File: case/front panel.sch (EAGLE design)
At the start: 3 parts

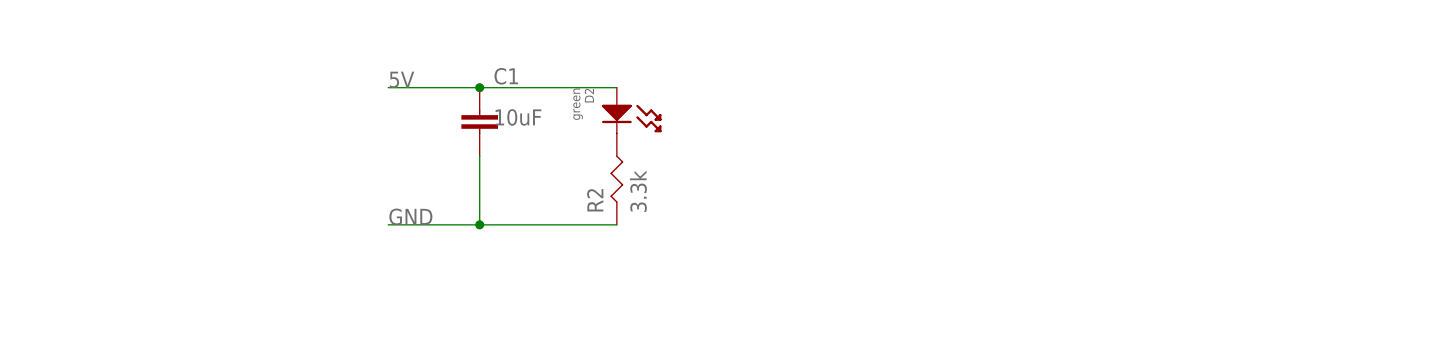
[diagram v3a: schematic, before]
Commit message: add rgb leds
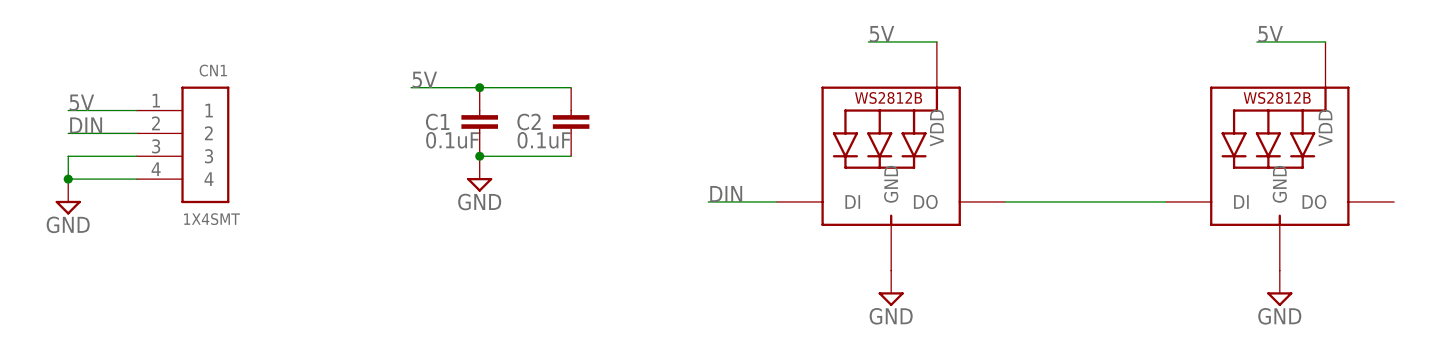
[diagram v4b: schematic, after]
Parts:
- removed D2: green, MF_LEDs:LED_SINGLE-0805
- removed R2: 3.3k, FlashPCB_Resistors:RES-0402
- added C2: 0.1uF, Nordic_nRF:CAPACITOR_0805_N
- added CN1: 1X4SMT, adafruit:1X4SMT
- added LED1, LED2: WS2812B_5050N, adafruit:WS2812B_5050N
- C1: value 10uF -> 0.1uF
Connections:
- new net DIN: CN1.2, LED1.DI
- net 5V: now also C2.1, CN1.1, LED1.VDD, LED2.VDD; no longer D2.ANODE
- net GND: now also C2.2, CN1.3, CN1.4, LED1.GND, LED2.GND; no longer R2.P$1
- net N$2: now also LED1.DO, LED2.DI; no longer D2.CATHODE, R2.P$2
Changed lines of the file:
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@@
 </classes>
 <parts>
-<part name="D2" library="MF_LEDs" deviceset="LED_SINGLE" device="-0805" value="green"/>
-<part name="R2" library="FlashPCB_Resistors" deviceset="RES-0402" device="" value="3.3k"/>
-<part name="C1" library="Nordic_nRF" library_urn="urn:adsk.eagle:library:169009" deviceset="CAPACITOR" device="_0805_N" package3d_urn="urn:adsk.eagle:package:2593736/1" value="10uF"/>
+<part name="C1" library="Nordic_nRF" library_urn="urn:adsk.eagle:library:169009" deviceset="CAPACITOR" device="_0805_N" package3d_urn="urn:adsk.eagle:package:2593736/1" value="0.1uF"/>
+<part name="LED1" library="adafruit" deviceset="WS2812B" device="_5050N"/>
+<part name="LED2" library="adafruit" deviceset="WS2812B" device="_5050N"/>
+<part name="SUPPLY1" library="Power_Symbols" library_urn="urn:adsk.eagle:library:16502351" deviceset="GND" device="" value="GND"/>
+<part name="SUPPLY2" library="Power_Symbols" library_urn="urn:adsk.eagle:library:16502351" deviceset="GND" device="" value="GND"/>
+<part name="SUPPLY3" library="Power_Symbols" library_urn="urn:adsk.eagle:library:16502351" deviceset="GND" device="" value="GND"/>
+<part name="CN1" library="adafruit" deviceset="1X4" device="SMT"/>
+<part name="SUPPLY4" library="Power_Symbols" library_urn="urn:adsk.eagle:library:16502351" deviceset="GND" device="" value="GND"/>
+<part name="C2" library="Nordic_nRF" library_urn="urn:adsk.eagle:library:169009" deviceset="CAPACITOR" device="_0805_N" package3d_urn="urn:adsk.eagle:package:2593736/1" value="0.1uF"/>
 </parts>
 <sheets>
@@
 </plain>
 <instances>
-<instance part="D2" gate="G$1" x="38.1" y="27.94" smashed="yes" rot="R270">
-<attribute name="NAME" x="35.56" y="30.48" size="1.016" layer="95" font="vector" rot="R270" align="top-left"/>
-<attribute name="VALUE" x="33.02" y="30.48" size="1.016" layer="96" font="vector" rot="R270"/>
+<instance part="C1" gate="C$1" x="22.86" y="27.94" smashed="yes">
+<attribute name="NAME" x="16.764" y="25.781" size="1.778" layer="95"/>
+<attribute name="VALUE" x="16.764" y="23.749" size="1.778" layer="96"/>
 </instance>
-<instance part="R2" gate="G$1" x="38.1" y="20.32" smashed="yes" rot="R90">
-<attribute name="NAME" x="36.6014" y="16.51" size="1.778" layer="95" rot="R90"/>
-<attribute name="VALUE" x="41.402" y="16.51" size="1.778" layer="96" rot="R90"/>
+<instance part="LED1" gate="G$1" x="68.58" y="20.32" smashed="yes"/>
+<instance part="LED2" gate="G$1" x="111.76" y="20.32" smashed="yes"/>
+<instance part="SUPPLY1" gate="G$1" x="22.86" y="20.32" smashed="yes">
+<attribute name="VALUE" x="22.86" y="17.78" size="1.778" layer="96" align="center"/>
 </instance>
-<instance part="C1" gate="C$1" x="22.86" y="27.94" smashed="yes">
-<attribute name="NAME" x="24.384" y="30.861" size="1.778" layer="95"/>
-<attribute name="VALUE" x="24.384" y="26.289" size="1.778" layer="96"/>
+<instance part="SUPPLY2" gate="G$1" x="68.58" y="7.62" smashed="yes">
+<attribute name="VALUE" x="68.58" y="5.08" size="1.778" layer="96" align="center"/>
+</instance>
+<instance part="SUPPLY3" gate="G$1" x="111.76" y="7.62" smashed="yes">
+<attribute name="VALUE" x="111.76" y="5.08" size="1.778" layer="96" align="center"/>
+</instance>
+<instance part="CN1" gate="G$1" x="-10.16" y="25.4" smashed="yes">
+<attribute name="NAME" x="-5.08" y="33.02" size="1.27" layer="95" font="vector" rot="R180"/>
+<attribute name="VALUE" x="-10.16" y="15.24" size="1.27" layer="96" font="vector"/>
+</instance>
+<instance part="SUPPLY4" gate="G$1" x="-22.86" y="17.78" smashed="yes">
+<attribute name="VALUE" x="-22.86" y="15.24" size="1.778" layer="96" align="center"/>
+</instance>
+<instance part="C2" gate="C$1" x="33.02" y="27.94" smashed="yes">
+<attribute name="NAME" x="26.924" y="25.781" size="1.778" layer="95"/>
+<attribute name="VALUE" x="26.924" y="23.749" size="1.778" layer="96"/>
 </instance>
 </instances>
@@
 <net name="GND" class="0">
 <segment>
-<pinref part="R2" gate="G$1" pin="P$1"/>
-<wire x1="38.1" y1="15.24" x2="22.86" y2="15.24" width="0.1524" layer="91"/>
-<wire x1="22.86" y1="15.24" x2="12.7" y2="15.24" width="0.1524" layer="91"/>
-<wire x1="22.86" y1="22.86" x2="22.86" y2="15.24" width="0.1524" layer="91"/>
-<junction x="22.86" y="15.24"/>
 <pinref part="C1" gate="C$1" pin="2"/>
-<label x="12.7" y="15.24" size="1.778" layer="95"/>
+<pinref part="SUPPLY1" gate="G$1" pin="GND"/>
+<pinref part="C2" gate="C$1" pin="2"/>
+<wire x1="33.02" y1="22.86" x2="22.86" y2="22.86" width="0.1524" layer="91"/>
+<junction x="22.86" y="22.86"/>
+</segment>
+<segment>
+<pinref part="LED1" gate="G$1" pin="GND"/>
+<pinref part="SUPPLY2" gate="G$1" pin="GND"/>
+</segment>
+<segment>
+<pinref part="LED2" gate="G$1" pin="GND"/>
+<pinref part="SUPPLY3" gate="G$1" pin="GND"/>
+</segment>
+<segment>
+<pinref part="CN1" gate="G$1" pin="4"/>
+<wire x1="-15.24" y1="20.32" x2="-22.86" y2="20.32" width="0.1524" layer="91"/>
+<pinref part="SUPPLY4" gate="G$1" pin="GND"/>
+<pinref part="CN1" gate="G$1" pin="3"/>
+<wire x1="-15.24" y1="22.86" x2="-22.86" y2="22.86" width="0.1524" layer="91"/>
+<wire x1="-22.86" y1="22.86" x2="-22.86" y2="20.32" width="0.1524" layer="91"/>
+<junction x="-22.86" y="20.32"/>
 </segment>
 </net>
 <net name="5V" class="0">
 <segment>
-<pinref part="D2" gate="G$1" pin="ANODE"/>
-<wire x1="38.1" y1="30.48" x2="22.86" y2="30.48" width="0.1524" layer="91"/>
 <pinref part="C1" gate="C$1" pin="1"/>
-<wire x1="22.86" y1="30.48" x2="12.7" y2="30.48" width="0.1524" layer="91"/>
+<wire x1="22.86" y1="30.48" x2="15.24" y2="30.48" width="0.1524" layer="91"/>
+<label x="15.24" y="30.48" size="1.778" layer="95"/>
+<pinref part="C2" gate="C$1" pin="1"/>
+<wire x1="22.86" y1="30.48" x2="33.02" y2="30.48" width="0.1524" layer="91"/>
 <junction x="22.86" y="30.48"/>
-<label x="12.7" y="30.48" size="1.778" layer="95"/>
 </segment>
-</net>
-<net name="N$1" class="0">
+<segment>
+<pinref part="LED2" gate="G$1" pin="VDD"/>
+<wire x1="116.84" y1="35.56" x2="109.22" y2="35.56" width="0.1524" layer="91"/>
+<label x="109.22" y="35.56" size="1.778" layer="95"/>
+</segment>
+<segment>
+<pinref part="LED1" gate="G$1" pin="VDD"/>
+<wire x1="73.66" y1="35.56" x2="66.04" y2="35.56" width="0.1524" layer="91"/>
+<label x="66.04" y="35.56" size="1.778" layer="95"/>
+</segment>
+<segment>
+<pinref part="CN1" gate="G$1" pin="1"/>
+<wire x1="-15.24" y1="27.94" x2="-22.86" y2="27.94" width="0.1524" layer="91"/>
+<label x="-22.86" y="27.94" size="1.778" layer="95"/>
+</segment>
 </net>
 <net name="N$2" class="0">
 <segment>
-<pinref part="R2" gate="G$1" pin="P$2"/>
-<pinref part="D2" gate="G$1" pin="CATHODE"/>
+<pinref part="LED1" gate="G$1" pin="DO"/>
+<pinref part="LED2" gate="G$1" pin="DI"/>
+<wire x1="81.28" y1="17.78" x2="99.06" y2="17.78" width="0.1524" layer="91"/>
 </segment>
 </net>
+<net name="DIN" class="0">
+<segment>
+<pinref part="CN1" gate="G$1" pin="2"/>
+<wire x1="-15.24" y1="25.4" x2="-22.86" y2="25.4" width="0.1524" layer="91"/>
+<label x="-22.86" y="25.4" size="1.778" layer="95"/>
+</segment>
+<segment>
+<pinref part="LED1" gate="G$1" pin="DI"/>
+<wire x1="55.88" y1="17.78" x2="48.26" y2="17.78" width="0.1524" layer="91"/>
+<label x="48.26" y="17.78" size="1.778" layer="95"/>
+</segment>
+</net>

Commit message: use SK6812MINI-E leds
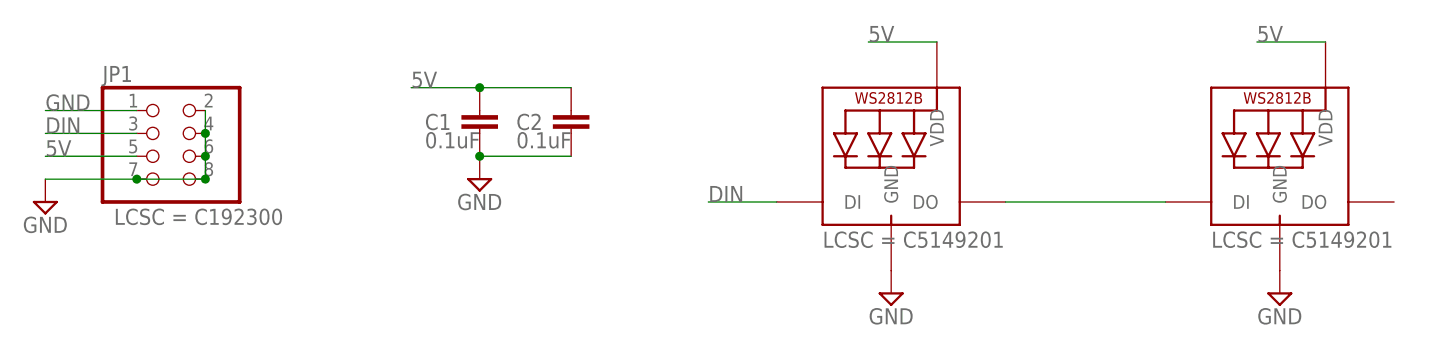
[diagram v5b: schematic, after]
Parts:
- removed CN1: 1X4SMT, adafruit:1X4SMT
- removed LED2: WS2812B_5050N, adafruit:WS2812B_5050N
- added JP1: connect, pinhead+:PINHD-2X4SMT
- added LED0: WS2812B_SK6812E, microbuilder:WS2812B_SK6812E
- LED1: value WS2812B_5050N -> WS2812B_SK6812E; device adafruit:WS2812B_5050N -> microbuilder:WS2812B_SK6812E; LCSC (none) -> C5149201
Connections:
- net 5V: now also JP1.5, LED0.VDD; no longer CN1.1, LED2.VDD
- net DIN: now also JP1.3; no longer CN1.2
- net GND: now also JP1.1, JP1.2, JP1.4, JP1.6, JP1.7, JP1.8, LED0.GND; no longer CN1.3, CN1.4, LED2.GND
- net N$2: now also LED0.DI; no longer LED2.DI
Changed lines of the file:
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@@
 <layer number="59" name="tCarbon" color="7" fill="1" visible="no" active="no"/>
 <layer number="60" name="bCarbon" color="7" fill="1" visible="no" active="no"/>
+<layer number="61" name="stand" color="7" fill="1" visible="no" active="no"/>
 <layer number="88" name="SimResults" color="9" fill="1" visible="yes" active="yes"/>
 <layer number="89" name="SimProbes" color="9" fill="1" visible="yes" active="yes"/>
@@
 <parts>
 <part name="C1" library="Nordic_nRF" library_urn="urn:adsk.eagle:library:169009" deviceset="CAPACITOR" device="_0805_N" package3d_urn="urn:adsk.eagle:package:2593736/1" value="0.1uF"/>
-<part name="LED1" library="adafruit" deviceset="WS2812B" device="_5050N"/>
-<part name="LED2" library="adafruit" deviceset="WS2812B" device="_5050N"/>
 <part name="SUPPLY1" library="Power_Symbols" library_urn="urn:adsk.eagle:library:16502351" deviceset="GND" device="" value="GND"/>
 <part name="SUPPLY2" library="Power_Symbols" library_urn="urn:adsk.eagle:library:16502351" deviceset="GND" device="" value="GND"/>
 <part name="SUPPLY3" library="Power_Symbols" library_urn="urn:adsk.eagle:library:16502351" deviceset="GND" device="" value="GND"/>
-<part name="CN1" library="adafruit" deviceset="1X4" device="SMT"/>
 <part name="SUPPLY4" library="Power_Symbols" library_urn="urn:adsk.eagle:library:16502351" deviceset="GND" device="" value="GND"/>
 <part name="C2" library="Nordic_nRF" library_urn="urn:adsk.eagle:library:169009" deviceset="CAPACITOR" device="_0805_N" package3d_urn="urn:adsk.eagle:package:2593736/1" value="0.1uF"/>
+<part name="LED1" library="microbuilder" deviceset="WS2812B" device="_SK6812E">
+<attribute name="LCSC" value="C5149201"/>
+</part>
+<part name="LED0" library="microbuilder" deviceset="WS2812B" device="_SK6812E">
+<attribute name="LCSC" value="C5149201"/>
+</part>
+<part name="JP1" library="pinhead+" deviceset="PINHD-2X4" device="SMT" value="connect">
+<attribute name="LCSC" value="C192300"/>
+</part>
 </parts>
 <sheets>
@@
 <attribute name="VALUE" x="16.764" y="23.749" size="1.778" layer="96"/>
 </instance>
-<instance part="LED1" gate="G$1" x="68.58" y="20.32" smashed="yes"/>
-<instance part="LED2" gate="G$1" x="111.76" y="20.32" smashed="yes"/>
 <instance part="SUPPLY1" gate="G$1" x="22.86" y="20.32" smashed="yes">
 <attribute name="VALUE" x="22.86" y="17.78" size="1.778" layer="96" align="center"/>
@@
 <attribute name="VALUE" x="111.76" y="5.08" size="1.778" layer="96" align="center"/>
 </instance>
-<instance part="CN1" gate="G$1" x="-10.16" y="25.4" smashed="yes">
-<attribute name="NAME" x="-5.08" y="33.02" size="1.27" layer="95" font="vector" rot="R180"/>
-<attribute name="VALUE" x="-10.16" y="15.24" size="1.27" layer="96" font="vector"/>
-</instance>
-<instance part="SUPPLY4" gate="G$1" x="-22.86" y="17.78" smashed="yes">
-<attribute name="VALUE" x="-22.86" y="15.24" size="1.778" layer="96" align="center"/>
+<instance part="SUPPLY4" gate="G$1" x="-25.4" y="17.78" smashed="yes">
+<attribute name="VALUE" x="-25.4" y="15.24" size="1.778" layer="96" align="center"/>
 </instance>
 <instance part="C2" gate="C$1" x="33.02" y="27.94" smashed="yes">
 <attribute name="NAME" x="26.924" y="25.781" size="1.778" layer="95"/>
 <attribute name="VALUE" x="26.924" y="23.749" size="1.778" layer="96"/>
+</instance>
+<instance part="LED1" gate="G$1" x="68.58" y="20.32" smashed="yes">
+<attribute name="LCSC" x="60.96" y="12.7" size="1.778" layer="96" display="both"/>
+</instance>
+<instance part="LED0" gate="G$1" x="111.76" y="20.32" smashed="yes">
+<attribute name="LCSC" x="104.14" y="12.7" size="1.778" layer="96" display="both"/>
+</instance>
+<instance part="JP1" gate="A" x="-12.7" y="22.86" smashed="yes">
+<attribute name="NAME" x="-19.05" y="31.115" size="1.778" layer="95"/>
+<attribute name="LCSC" x="-17.78" y="15.24" size="1.778" layer="96" display="both"/>
 </instance>
 </instances>
@@
 </segment>
 <segment>
+<wire x1="-15.24" y1="20.32" x2="-25.4" y2="20.32" width="0.1524" layer="91"/>
+<pinref part="SUPPLY4" gate="G$1" pin="GND"/>
+<pinref part="JP1" gate="A" pin="7"/>
+<pinref part="JP1" gate="A" pin="2"/>
+<pinref part="JP1" gate="A" pin="4"/>
+<wire x1="-7.62" y1="27.94" x2="-7.62" y2="25.4" width="0.1524" layer="91"/>
+<pinref part="JP1" gate="A" pin="6"/>
+<wire x1="-7.62" y1="25.4" x2="-7.62" y2="22.86" width="0.1524" layer="91"/>
+<junction x="-7.62" y="25.4"/>
+<pinref part="JP1" gate="A" pin="8"/>
+<wire x1="-7.62" y1="22.86" x2="-7.62" y2="20.32" width="0.1524" layer="91"/>
+<junction x="-7.62" y="22.86"/>
+<wire x1="-7.62" y1="20.32" x2="-15.24" y2="20.32" width="0.1524" layer="91"/>
+<junction x="-7.62" y="20.32"/>
+<junction x="-15.24" y="20.32"/>
+</segment>
+<segment>
 <pinref part="LED1" gate="G$1" pin="GND"/>
 <pinref part="SUPPLY2" gate="G$1" pin="GND"/>
 </segment>
 <segment>
-<pinref part="LED2" gate="G$1" pin="GND"/>
 <pinref part="SUPPLY3" gate="G$1" pin="GND"/>
-</segment>
-<segment>
-<pinref part="CN1" gate="G$1" pin="4"/>
-<wire x1="-15.24" y1="20.32" x2="-22.86" y2="20.32" width="0.1524" layer="91"/>
-<pinref part="SUPPLY4" gate="G$1" pin="GND"/>
-<pinref part="CN1" gate="G$1" pin="3"/>
-<wire x1="-15.24" y1="22.86" x2="-22.86" y2="22.86" width="0.1524" layer="91"/>
-<wire x1="-22.86" y1="22.86" x2="-22.86" y2="20.32" width="0.1524" layer="91"/>
-<junction x="-22.86" y="20.32"/>
+<pinref part="LED0" gate="G$1" pin="GND"/>
+</segment>
+<segment>
+<wire x1="-15.24" y1="27.94" x2="-25.4" y2="27.94" width="0.1524" layer="91"/>
+<label x="-25.4" y="27.94" size="1.778" layer="95"/>
+<pinref part="JP1" gate="A" pin="1"/>
 </segment>
 </net>
@@
 </segment>
 <segment>
-<pinref part="LED2" gate="G$1" pin="VDD"/>
 <wire x1="116.84" y1="35.56" x2="109.22" y2="35.56" width="0.1524" layer="91"/>
 <label x="109.22" y="35.56" size="1.778" layer="95"/>
-</segment>
-<segment>
-<pinref part="LED1" gate="G$1" pin="VDD"/>
+<pinref part="LED0" gate="G$1" pin="VDD"/>
+</segment>
+<segment>
 <wire x1="73.66" y1="35.56" x2="66.04" y2="35.56" width="0.1524" layer="91"/>
 <label x="66.04" y="35.56" size="1.778" layer="95"/>
-</segment>
-<segment>
-<pinref part="CN1" gate="G$1" pin="1"/>
-<wire x1="-15.24" y1="27.94" x2="-22.86" y2="27.94" width="0.1524" layer="91"/>
-<label x="-22.86" y="27.94" size="1.778" layer="95"/>
+<pinref part="LED1" gate="G$1" pin="VDD"/>
+</segment>
+<segment>
+<pinref part="JP1" gate="A" pin="5"/>
+<wire x1="-15.24" y1="22.86" x2="-25.4" y2="22.86" width="0.1524" layer="91"/>
+<label x="-25.4" y="22.86" size="1.778" layer="95"/>
 </segment>
 </net>
 <net name="N$2" class="0">
 <segment>
+<wire x1="81.28" y1="17.78" x2="99.06" y2="17.78" width="0.1524" layer="91"/>
 <pinref part="LED1" gate="G$1" pin="DO"/>
-<pinref part="LED2" gate="G$1" pin="DI"/>
-<wire x1="81.28" y1="17.78" x2="99.06" y2="17.78" width="0.1524" layer="91"/>
+<pinref part="LED0" gate="G$1" pin="DI"/>
 </segment>
 </net>
 <net name="DIN" class="0">
 <segment>
-<pinref part="CN1" gate="G$1" pin="2"/>
-<wire x1="-15.24" y1="25.4" x2="-22.86" y2="25.4" width="0.1524" layer="91"/>
-<label x="-22.86" y="25.4" size="1.778" layer="95"/>
-</segment>
-<segment>
-<pinref part="LED1" gate="G$1" pin="DI"/>
+<wire x1="-15.24" y1="25.4" x2="-25.4" y2="25.4" width="0.1524" layer="91"/>
+<label x="-25.4" y="25.4" size="1.778" layer="95"/>
+<pinref part="JP1" gate="A" pin="3"/>
+</segment>
+<segment>
 <wire x1="55.88" y1="17.78" x2="48.26" y2="17.78" width="0.1524" layer="91"/>
 <label x="48.26" y="17.78" size="1.778" layer="95"/>
-</segment>
-</net>
+<pinref part="LED1" gate="G$1" pin="DI"/>
+</segment>
+</net>
